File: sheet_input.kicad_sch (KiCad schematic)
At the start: 24 parts, among them J1 NCJ6FA-H, J5 VDD_PoE / PGND, Q1 DMP3098 (P-FET 60V), SW1 SS-12D00-G3

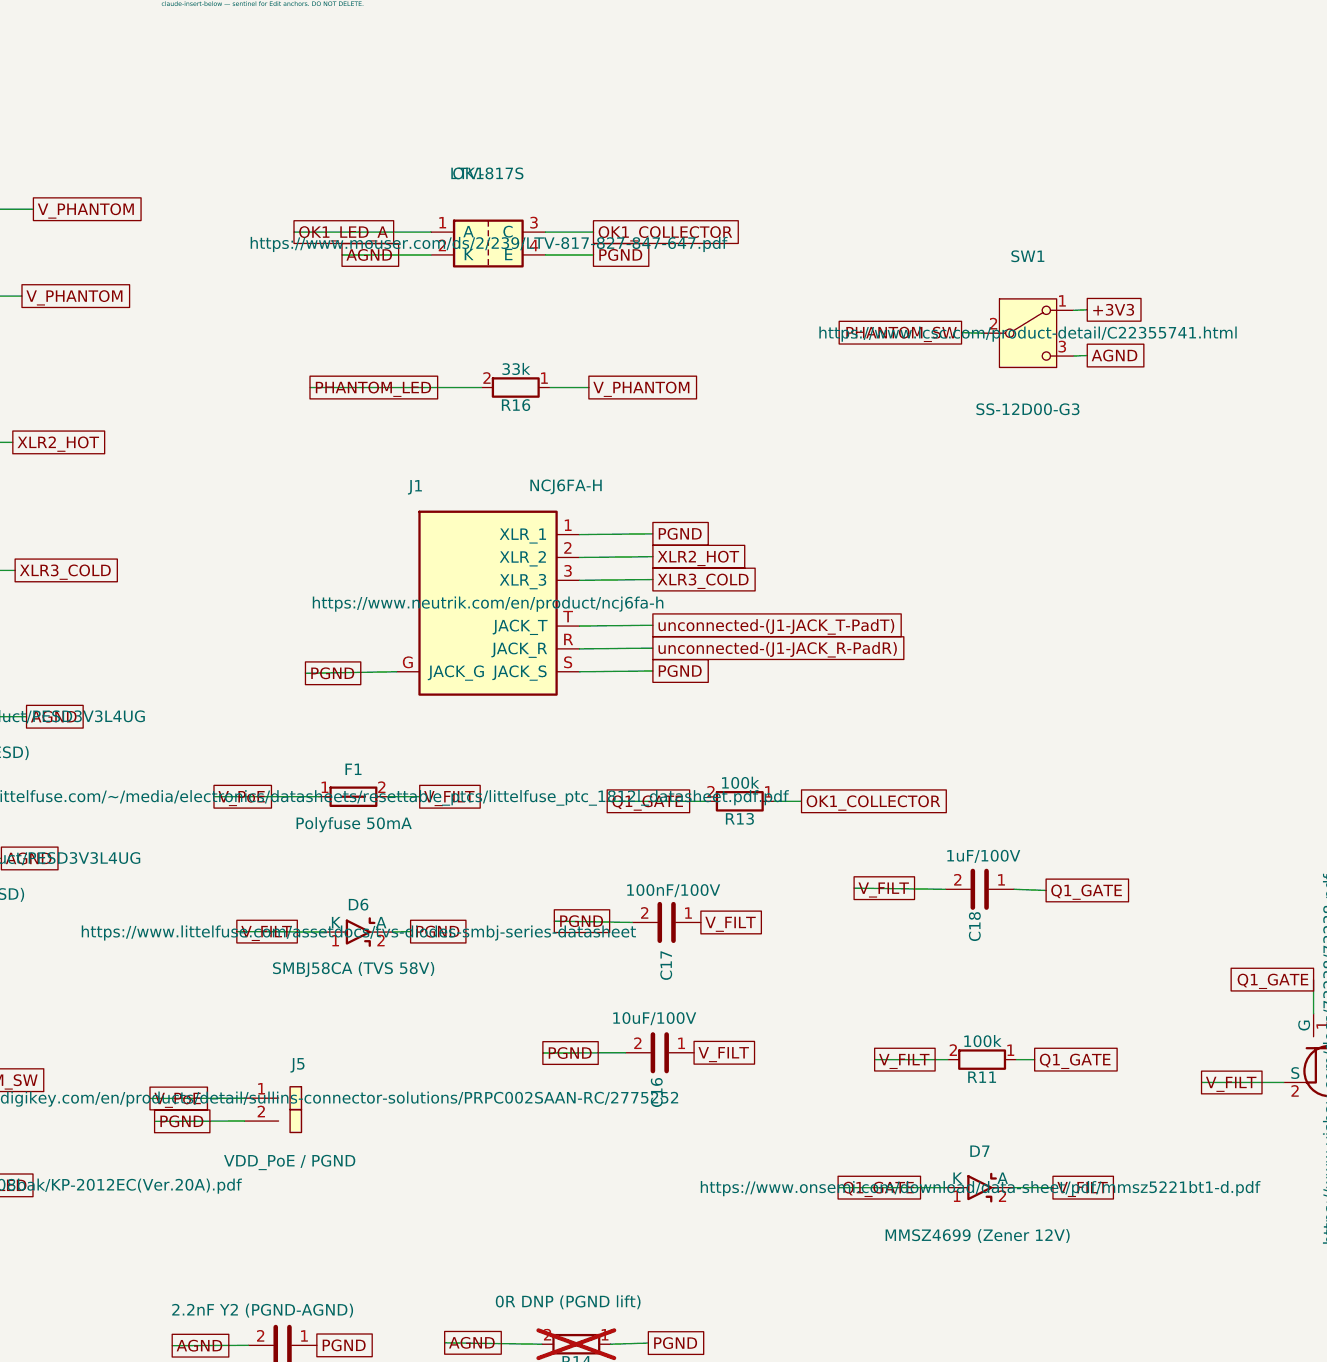
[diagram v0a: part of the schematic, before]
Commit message: fix: phantom drive — correct D7/OK1 orientation, 80V opto, drop C16
- D7 zener was reversed (Vgs clamped at -0.7V, FET never switched);
  cathode now to V_FILT, anode to Q1_GATE.
- OK1 optocoupler C/E were swapped in the symbol (pin3/pin4), exceeding
  its 6V emitter-collector reverse rating on the PoE rail and holding
  phantom on in both switch positions; collector->R13/gate, emitter->PGND.
- OK1 -> TLP291 (80V Vceo), SOP-4 1.27mm; LTV-817's 35V was under-rated
  for the 46-57V PoE rail.
- Remove C16 (10uF): it sat on the tapped bus and broke 802.3 PoE
  detection (>0.15uF), which blocked cold-start with the tap connected.
- Regenerate fab set (gerbers, drills, CPL, BOM) for the above.
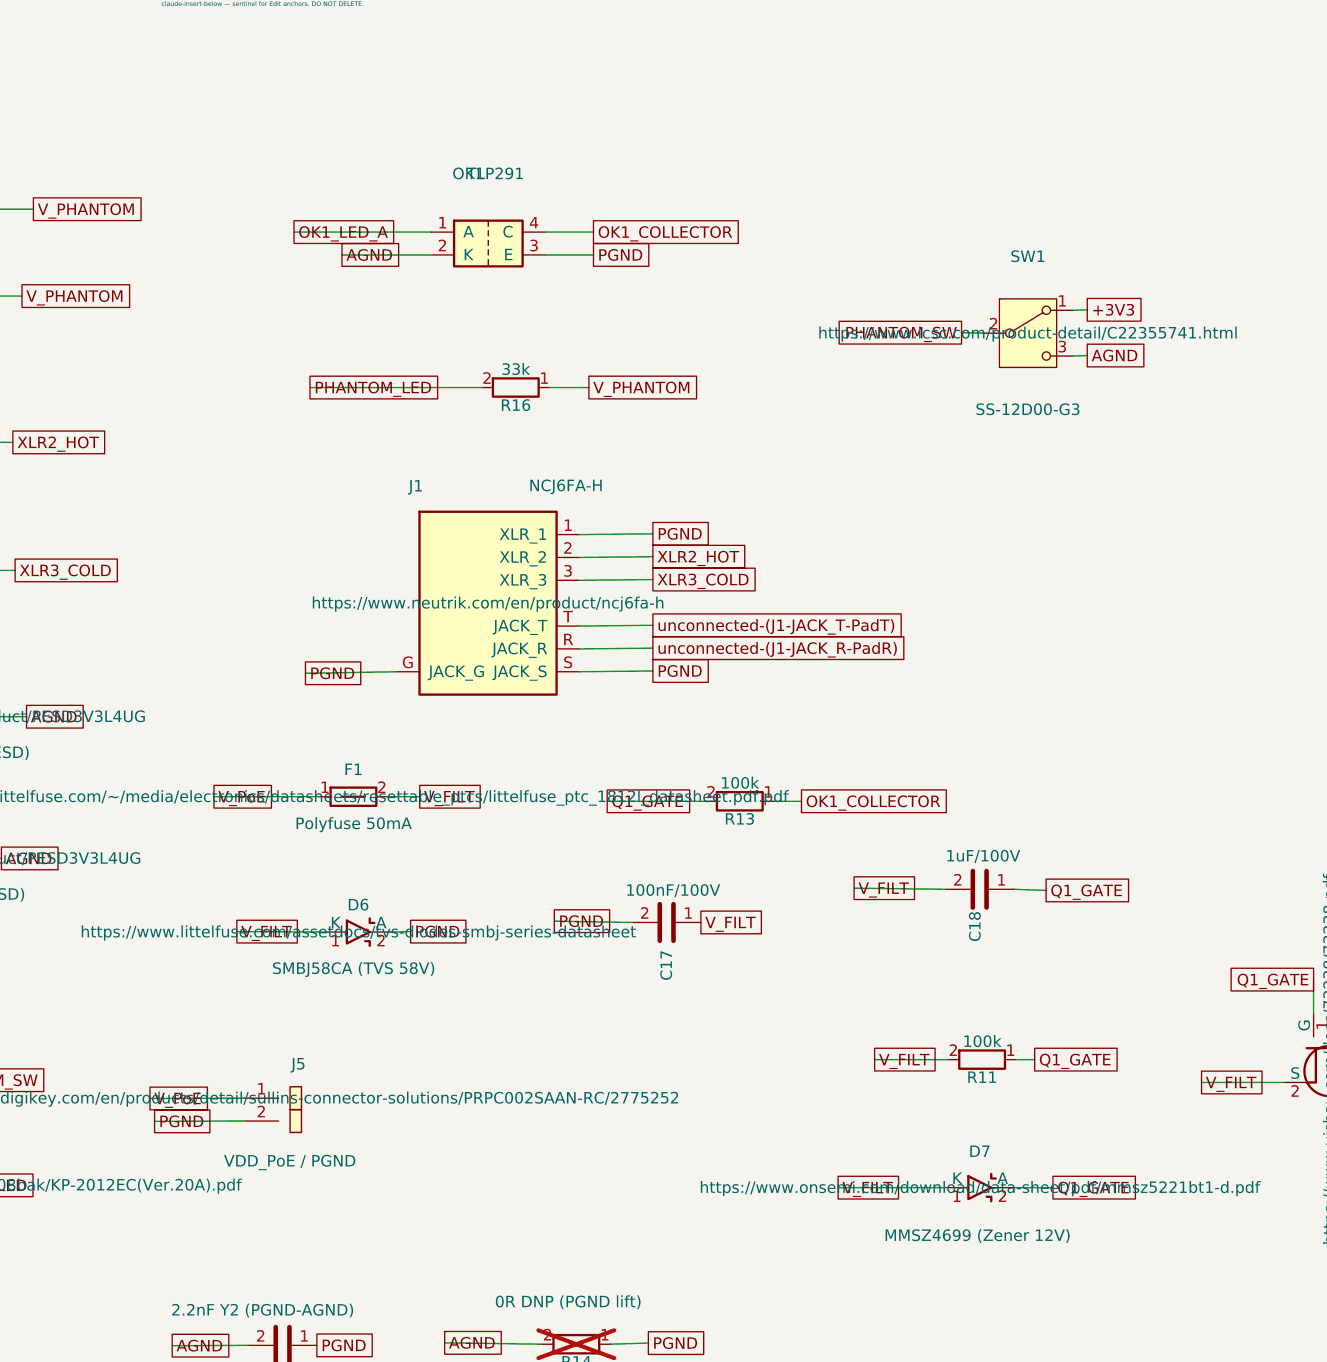
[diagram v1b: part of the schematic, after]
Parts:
- removed C16: 10uF/100V, Capacitor_SMD:C_1210_3225Metric, symbol scramble_hat:C
- OK1: value LTV-817S -> TLP291; footprint Package_SO:SO-4_7.6x3.6mm_P2.54mm -> Package_SO:SOP-4_4.4x2.6mm_P1.27mm
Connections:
- net OK1_COLLECTOR: now also OK1.4 (C); no longer OK1.3 (C)
- net PGND: now also OK1.3 (E); no longer OK1.4 (E)
- net Q1_GATE: now also D7.2 (A); no longer D7.1 (K)
- net V_FILT: now also D7.1 (K); no longer D7.2 (A)

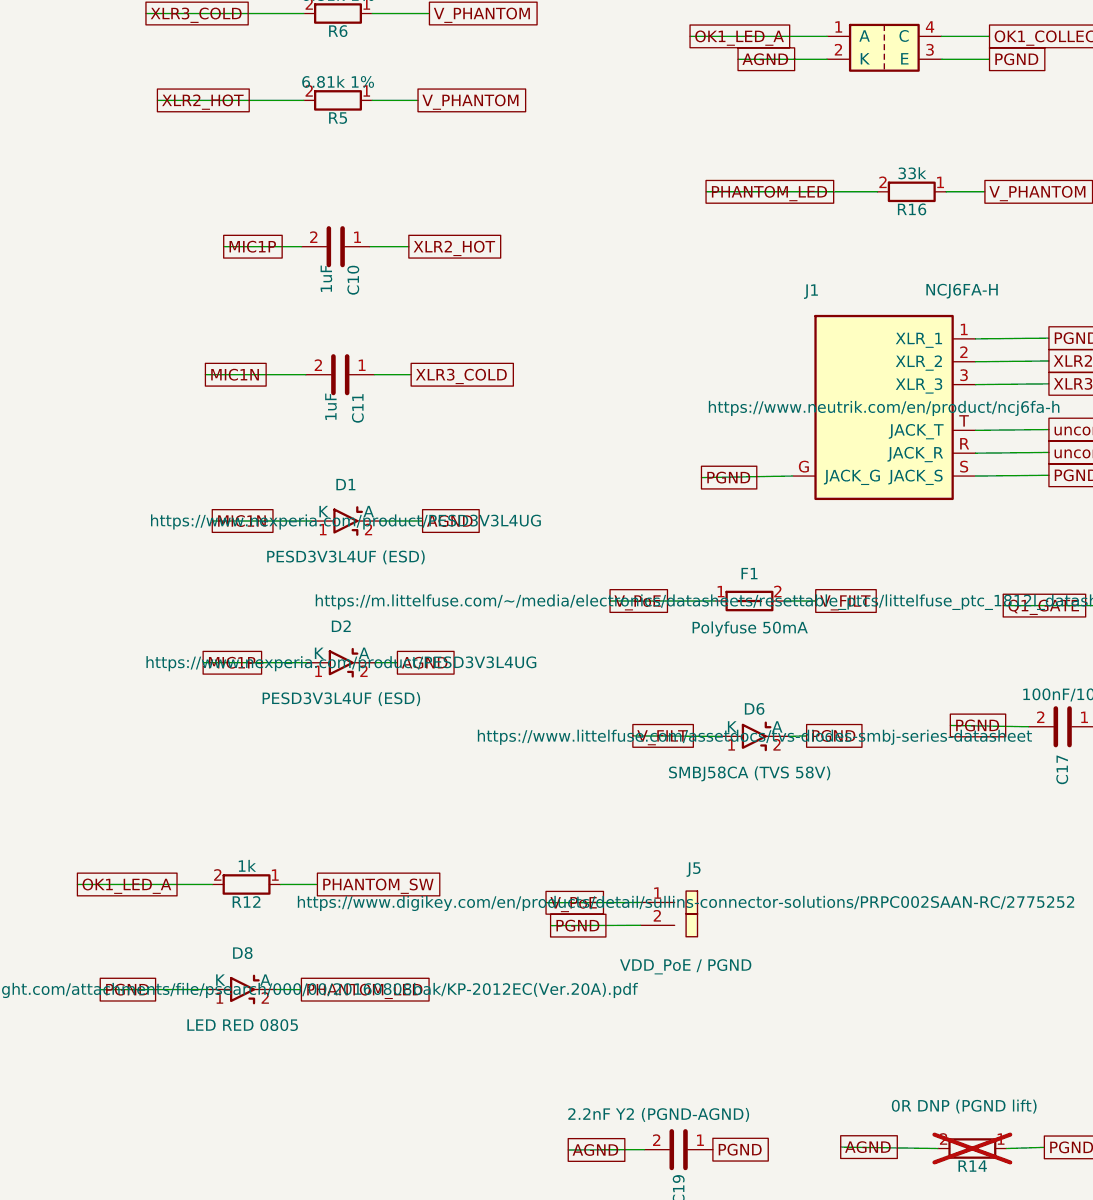
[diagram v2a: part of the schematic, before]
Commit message: fab: production prep — white/brighter status LED, C19 assembled, live BOM prices
- D8 red -> white: KT-0805W (C34499, Basic, in stock); old Kingbright
  KP-2012EC (C598272) was out of stock.
- R16 33k -> 15k, 1/4W AC0805 (C20142753) — ~2x brighter phantom-present
  LED (~3mA); resistor dissipates ~193mW at the 57V PoE max.
- C19 -> JEC JY222M2FY5VS7LE (C389727, Y2 300VAC, same 7.5mm land, in
  stock) moved onto JLCPCB THT assembly (off the hand-solder list).
- exclude_from_pos_files on J1/J2/J5 so placement/CPL leaves the
  hand-soldered parts (jacks + PoE header) to hand assembly.
- BOM: added J6, filled all resistor LCSC#s, refreshed unit prices to
  live qty-10 LCSC, corrected the D1/D2 entry.
- Regenerated gerbers/drills/BOM (csv+xlsx) with J6.
- Removed stale kicad-cli CPL — generate placement with the jlcpcb-tools
  plugin (set U1/QFN +270deg) and verify in JLCPCB preview before order.
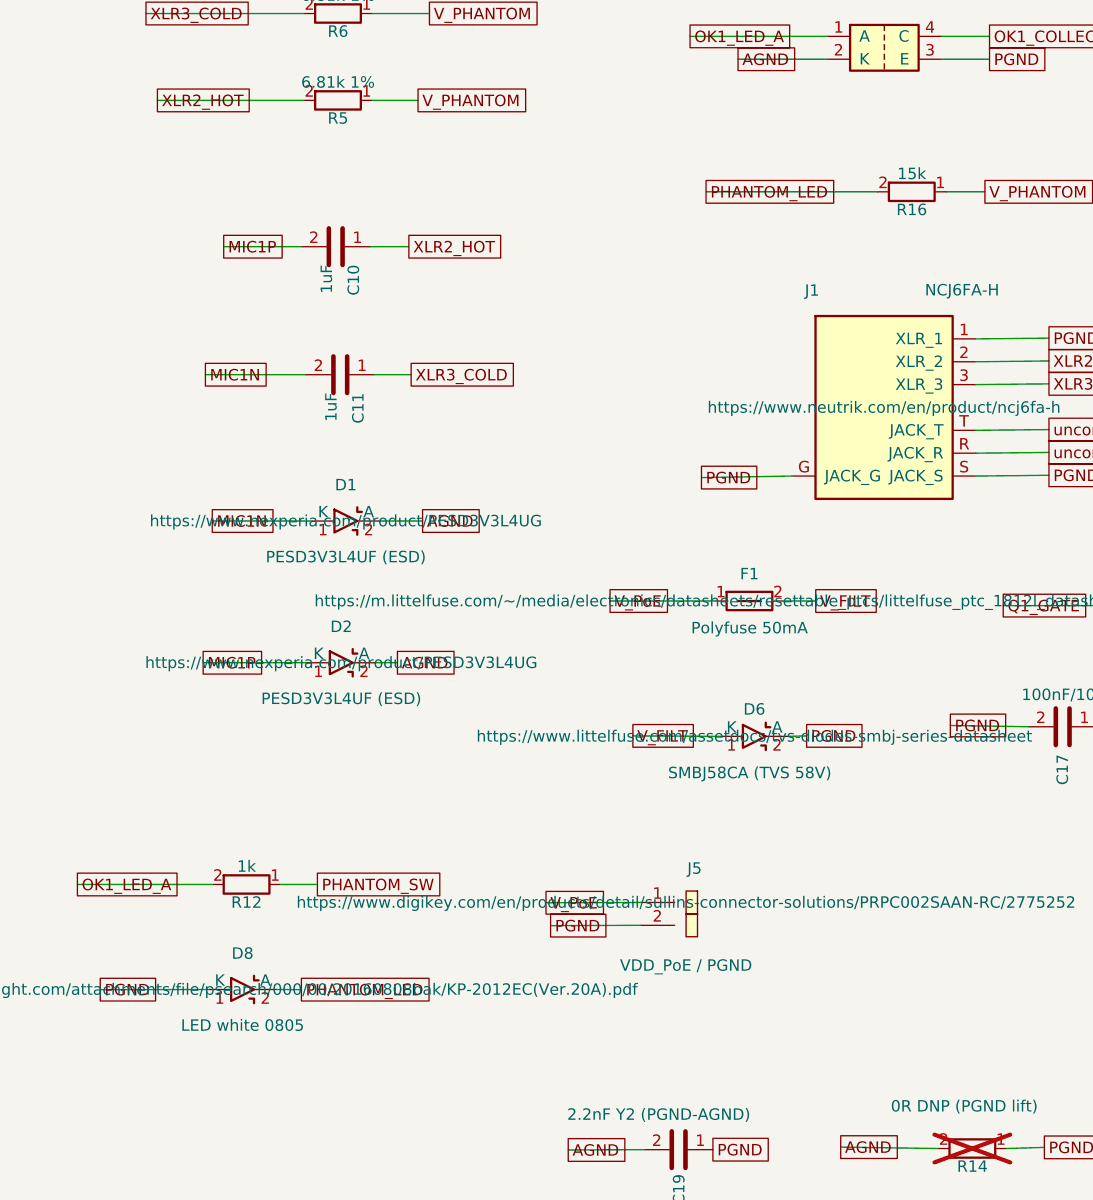
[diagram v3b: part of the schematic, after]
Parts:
- D8: value LED RED 0805 -> LED white 0805
- R16: value 33k -> 15k
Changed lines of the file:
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@@
 			)
 		)
-		(property "Value" "LED RED 0805"
+		(property "Value" "LED white 0805"
 			(at 168.722 158.67 0)
 			(show_name no)
@@
 			)
 		)
-		(property "Value" "33k"
+		(property "Value" "15k"
 			(at 243.078 64.04 90)
 			(show_name no)

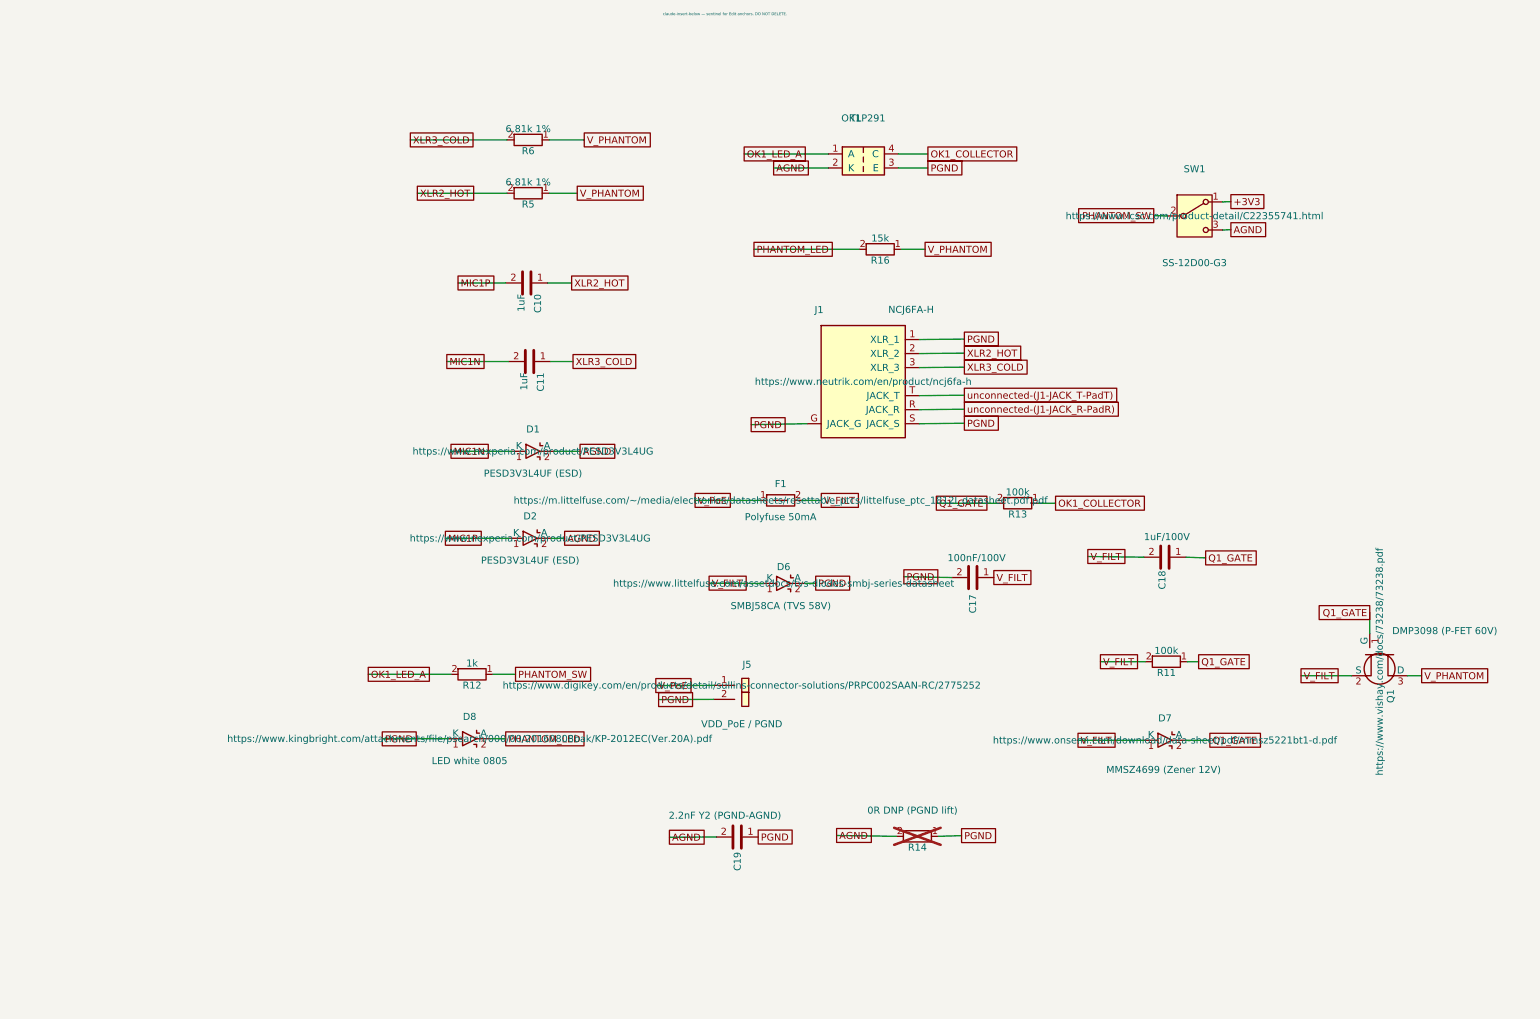
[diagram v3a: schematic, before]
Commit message: sch: add datasheet links, hide Datasheet/Description fields, remove sentinel text
- Filled 38 empty component Datasheet fields with LCSC product-page links (derived from the BOM part numbers); fixed D8's stale link (Kingbright KP-2012EC -> white KT-0805W / C34499). Existing manufacturer/distributor links kept.
- Hid the Datasheet and Description fields on all 53 placed components (most were previously shown, cluttering the canvas).
- Removed the 4 leftover sentinel text annotations.
- Netlist unchanged (check_sync: in sync, 53 comps / 46 nets).
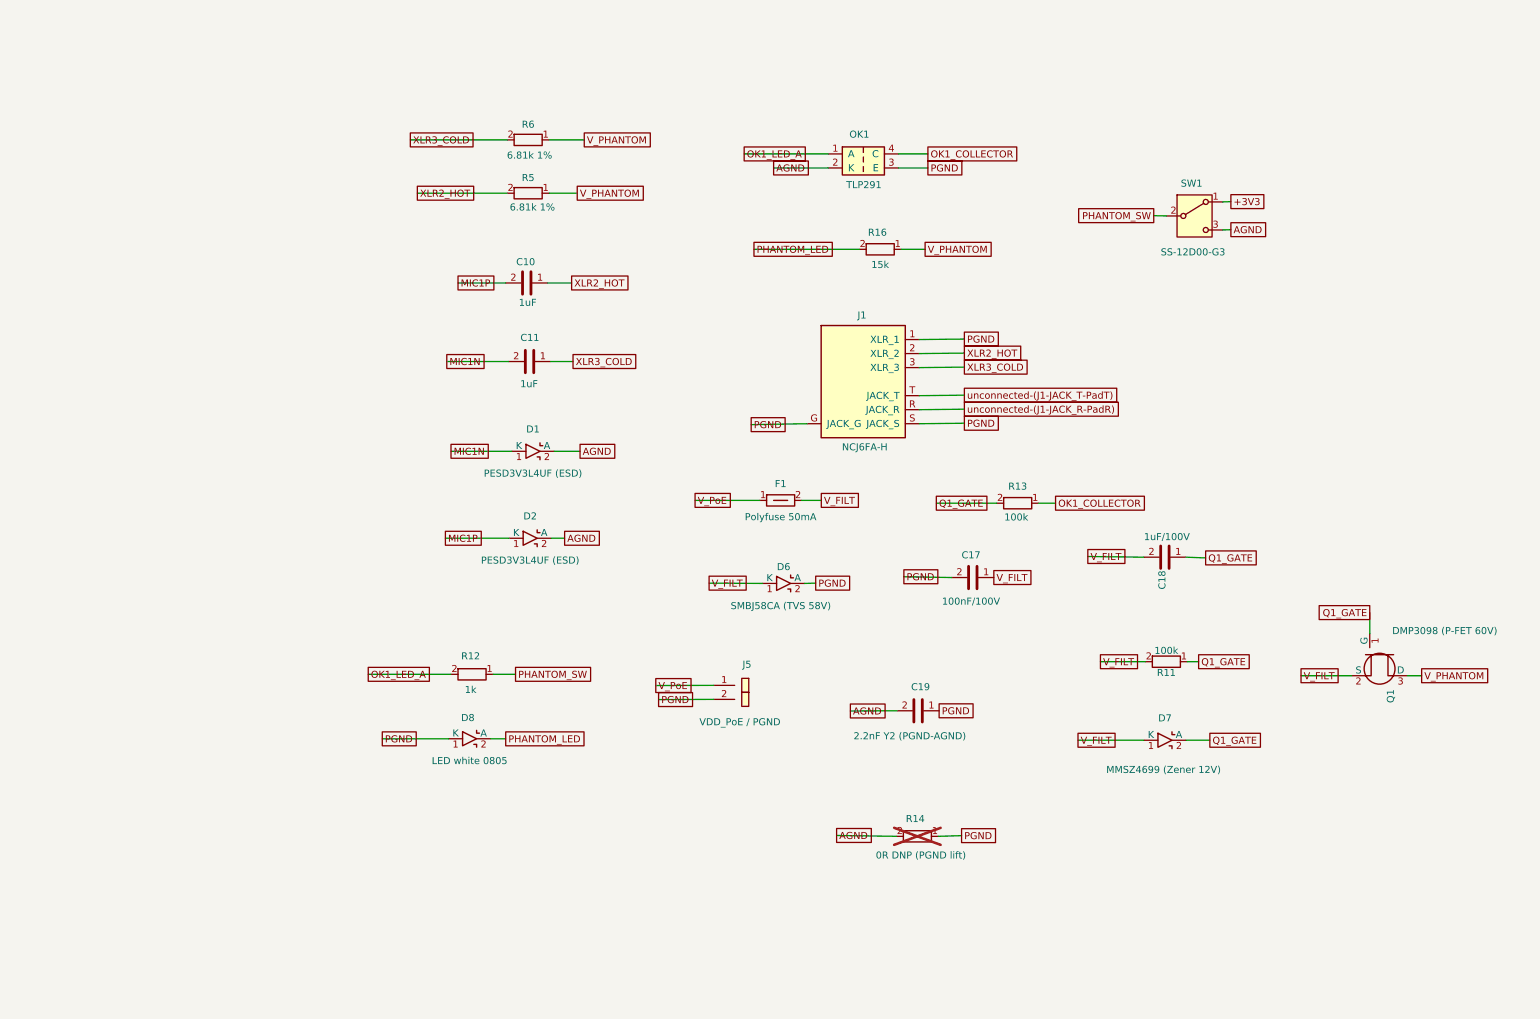
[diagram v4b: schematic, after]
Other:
- note removed: "claude-insert-below — sentinel for Edit anchors. DO NOT DELETE."
- moved on the sheet: C19
